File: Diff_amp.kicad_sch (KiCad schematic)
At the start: 15 parts, among them J1 Conn_01x01, J10 Conn_01x01, J2 Conn_01x01, J3 Conn_01x01, J4 Conn_01x01, J5 Conn_01x01, J6 Conn_01x01, J7 Conn_01x01, J8 Conn_01x01, J9 Conn_01x01, Q3 IRF540N, Q4 IRF540N

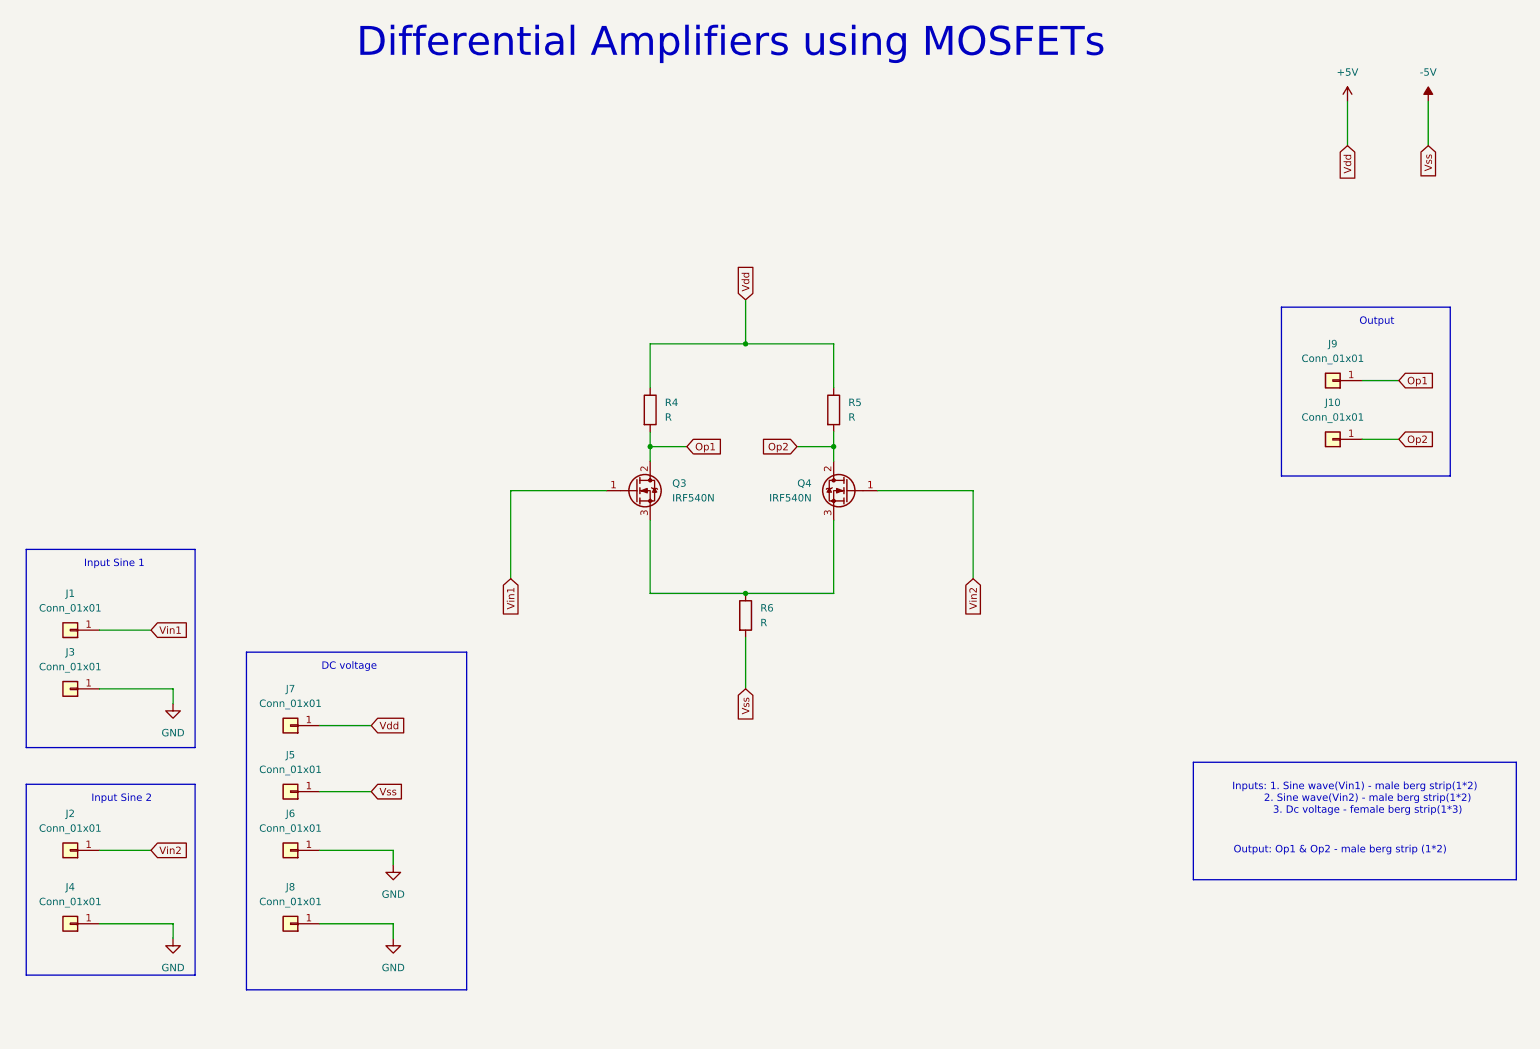
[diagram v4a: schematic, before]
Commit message: Edit-Annotations and ERC
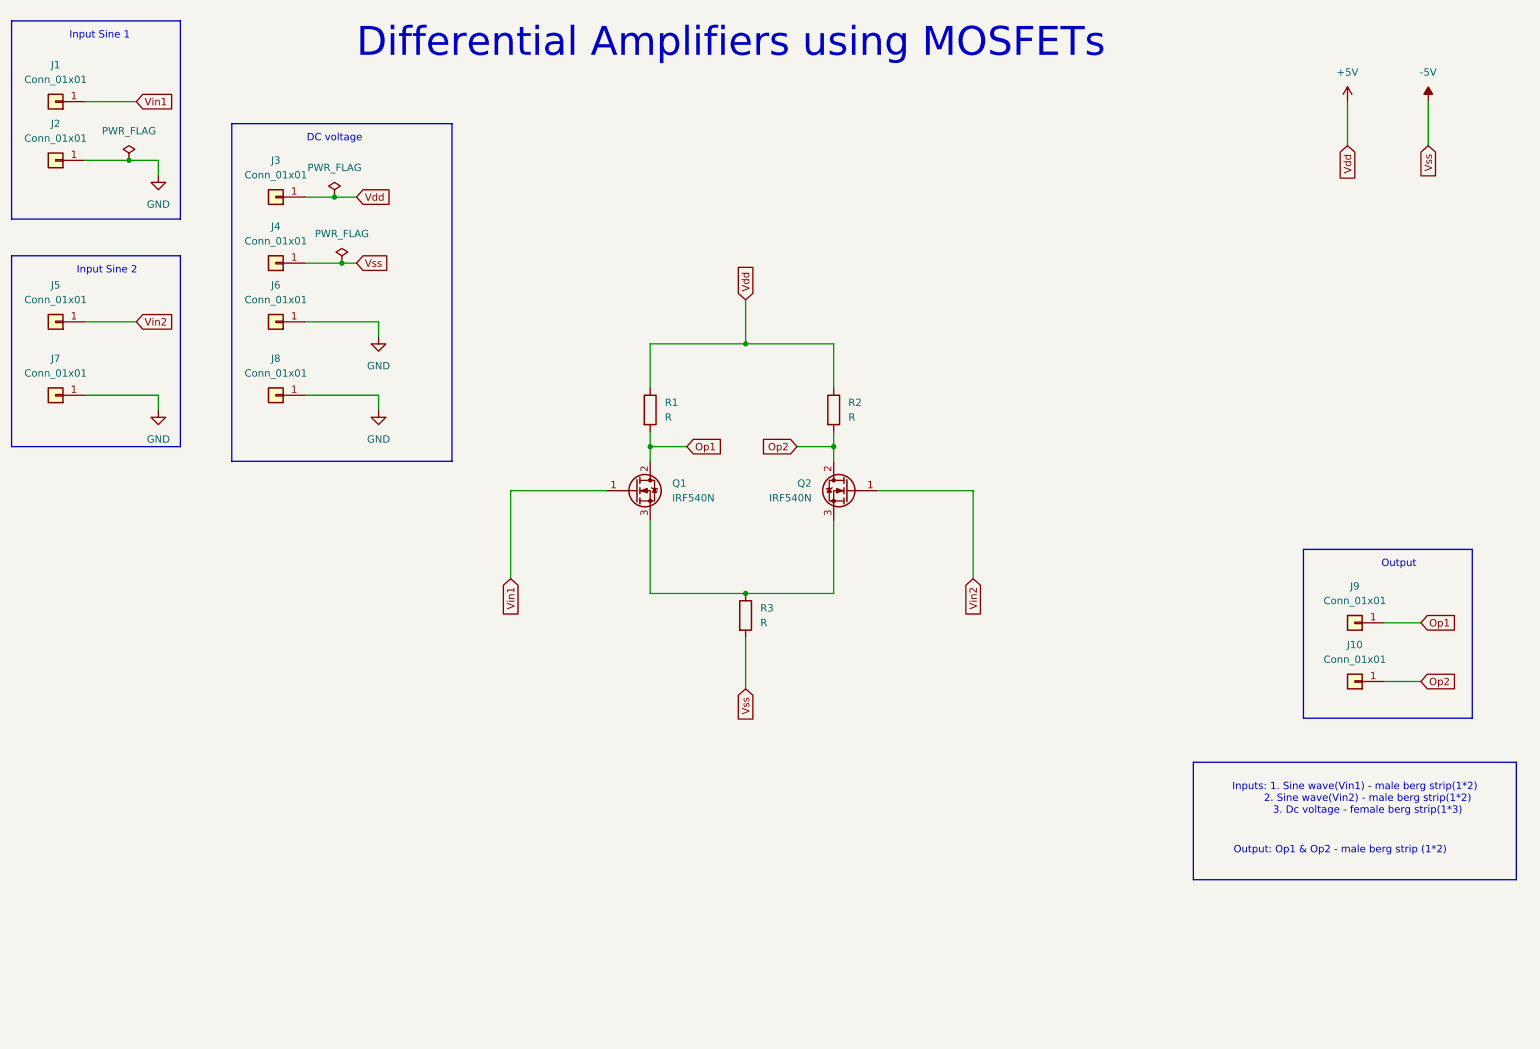
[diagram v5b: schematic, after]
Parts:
- renumbered J3 to J2, J7 to J3, J5 to J4, J2 to J5, J4 to J7, Q3 to Q1, Q4 to Q2, R4 to R1, R5 to R2, R6 to R3
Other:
- moved on the sheet: J1, J10, J2, J3, J4, J5, J6, J7, J8, J9

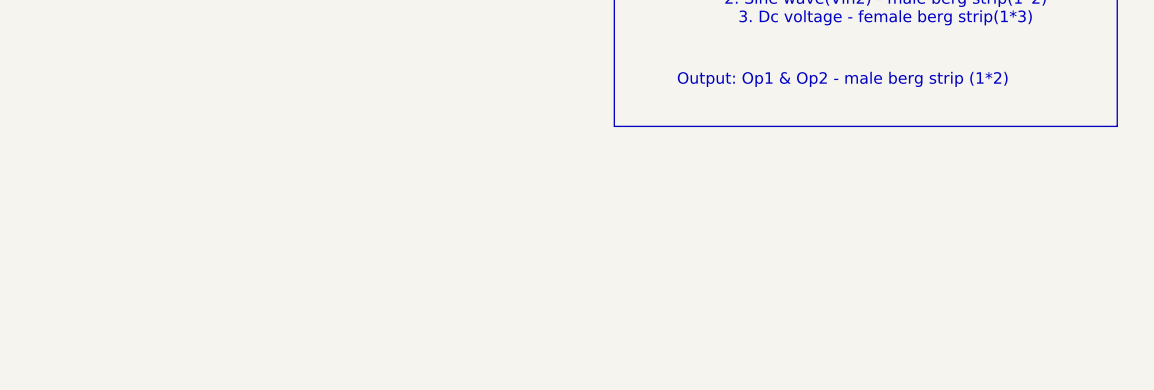
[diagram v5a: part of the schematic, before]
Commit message: Created BOM and ERC report
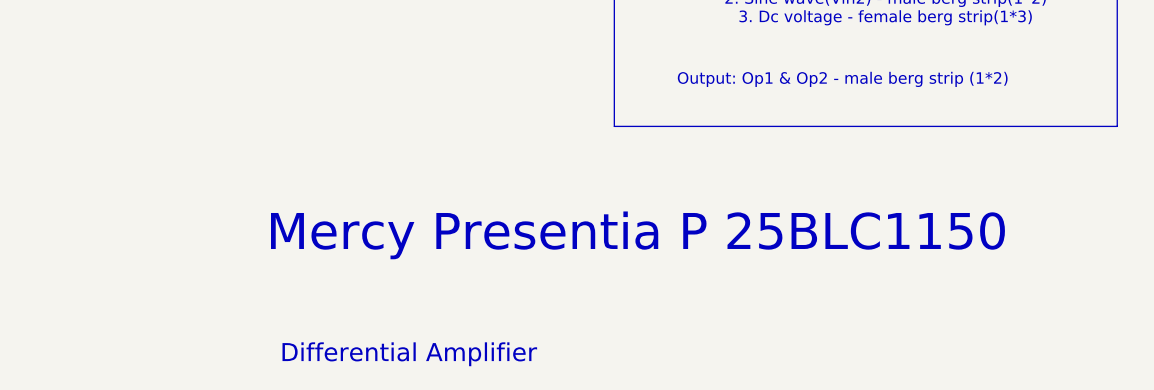
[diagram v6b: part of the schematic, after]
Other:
- note added: "Differential Amplifier"
- note added: "Mercy Presentia P 25BLC1150"
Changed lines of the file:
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@@
+		)
+	)
+	(text "Differential Amplifier\n"
+		(exclude_from_sim no)
+		(at 204.47 189.23 0)
+		(effects
+			(font
+				(size 2 2)
+			)
 		)
 	)
@@
 			)
 		)
+	)
+	(text "Mercy Presentia P 25BLC1150\n\n"
+		(exclude_from_sim no)
+		(at 229.87 179.07 0)
+		(effects
+			(font
+				(size 4 4)
+			)
+		)
